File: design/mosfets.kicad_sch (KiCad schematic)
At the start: 26 parts, among them Q1 IRFS7530, Q2 IRFS7530, Q3 IRFS7530, Q4 IRFS7530, Q5 IRFS7530, Q6 IRFS7530, U4 INA826AIDR, U6 OPA333AIDBVR, U7 INA826AIDR

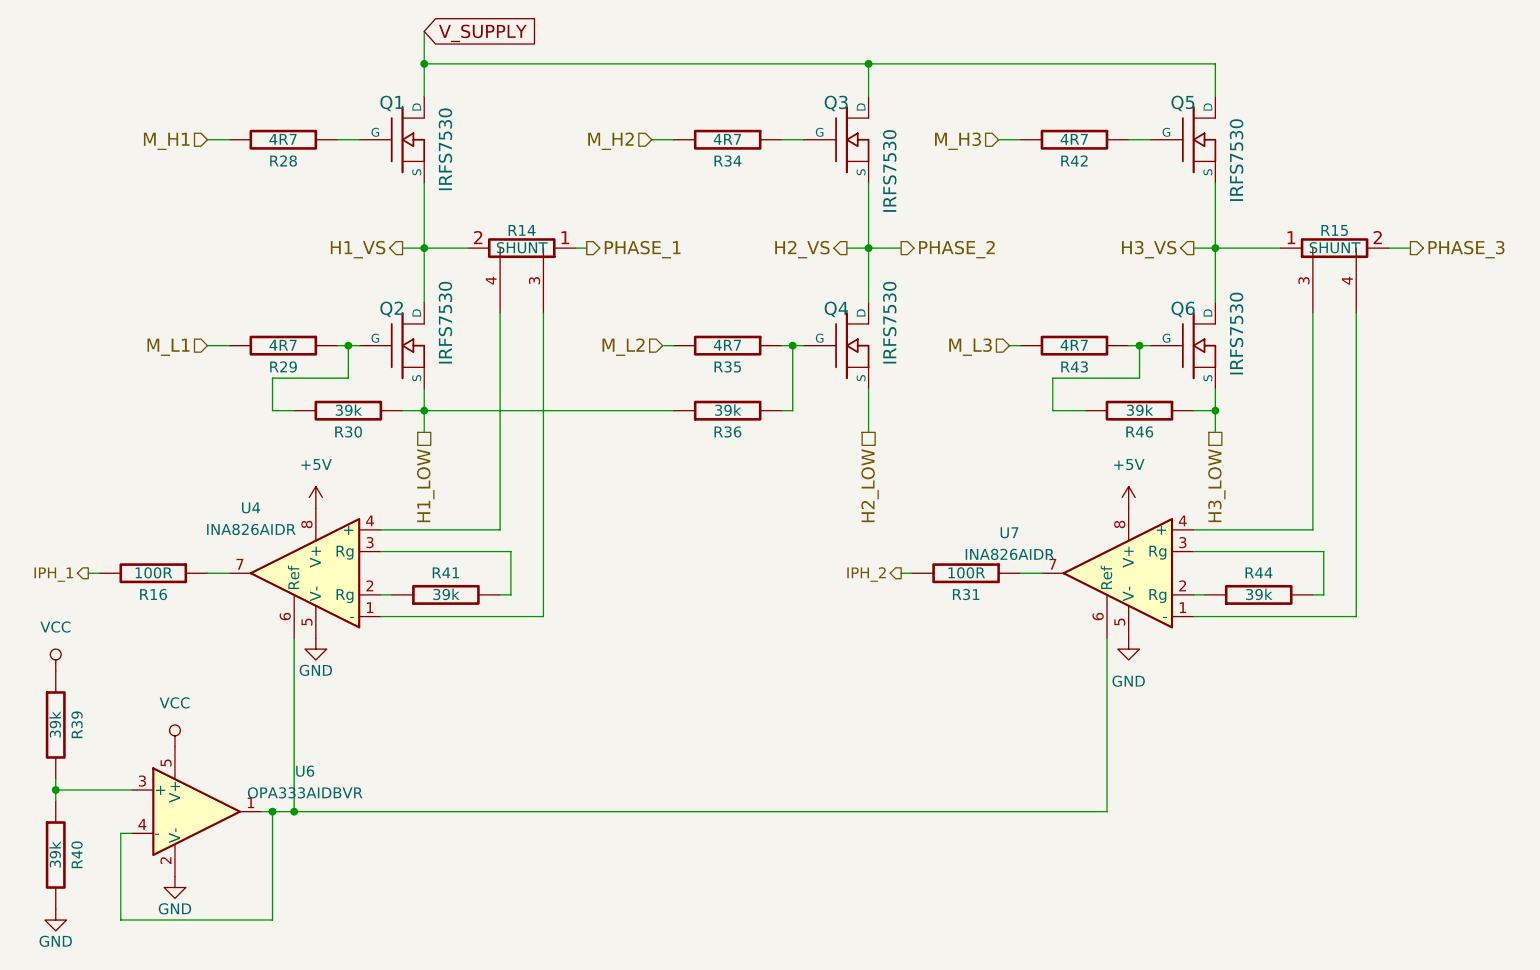
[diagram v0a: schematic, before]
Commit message: STM pins connected
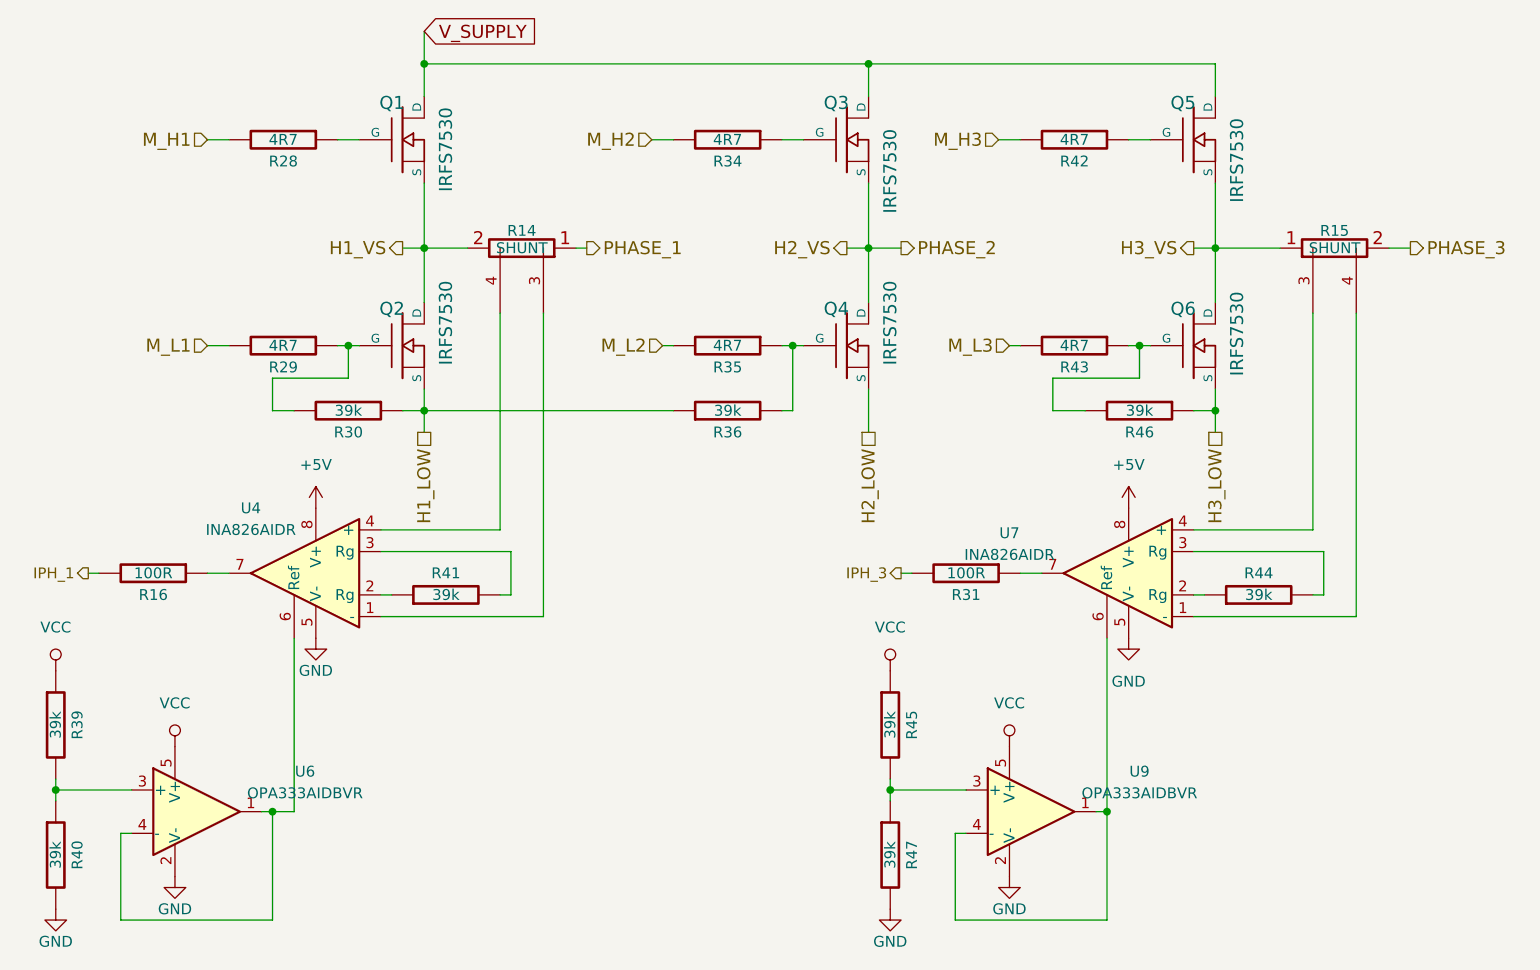
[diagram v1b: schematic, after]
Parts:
- added R45, R47: 39k, CRF1:SMD-0603_r, symbol BLDC_4-rescue:R-RESCUE-BLDC_4
- added U9: OPA333AIDBVR, Package_TO_SOT_SMD:SOT-23-5, symbol Amplifier_Operational:OPA333xxDBV
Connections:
- net GND: now also R47.2, U9.2 (V-)
- net VCC: now also R45.1, U9.5 (V+)
- net at U4.6 (Ref), U6.1, U6.4 (-): no longer U7.6 (Ref)
- net IPH_2 renamed IPH_3
- new net: U7.6 (Ref), U9.1, U9.4 (-)
- new net: R45.2, R47.1, U9.3 (+)

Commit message: Final 20230228
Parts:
- removed R14, R15: SHUNT, CRF1:WSLP2726, symbol BLDC_4-rescue:SHUNT
- added JP8 (x4): SolderJumper_2_Bridged, JRM_Footprint:MicroNetSep, symbol Jumper:SolderJumper_2_Bridged
- added R53 (x2): YLR12-3-8F-W, JRM_Footprint:YLR2512_G4, symbol Device:R_US
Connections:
- net H1_VS: now also JP8.2 (B), R53.1
- net H3_VS: now also JP8.2 (B), R53.1
- net PHASE_1: now also JP8.2 (B), R53.2
- net PHASE_3: now also JP8.2 (B), R53.2
- net at U7.1 (-): now also JP8.1 (A)
- net at U7.4 (+): now also JP8.1 (A)
- net at U4.1 (-): now also JP8.1 (A)
- net at U4.4 (+): now also JP8.1 (A)
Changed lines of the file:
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@@
     (company "Benjamin Vedder")
   )
+  (junction (at 123.19 83.82) (diameter 0) (color 0 0 0 0)
+  )
   (junction (at 115.57 102.87) (diameter 0) (color 0 0 0 0)
   )
@@
   (junction (at 115.57 83.82) (diameter 0) (color 0 0 0 0)
   )
+  (junction (at 130.81 83.82) (diameter 0) (color 0 0 0 0)
+  )
+  (junction (at 218.44 83.82) (diameter 0) (color 0 0 0 0)
+  )
   (junction (at 115.57 62.23) (diameter 0) (color 0 0 0 0)
   )
@@
   (junction (at 167.64 62.23) (diameter 0) (color 0 0 0 0)
   )
+  (junction (at 226.06 83.82) (diameter 0) (color 0 0 0 0)
+  )
   (junction (at 199.39 95.25) (diameter 0) (color 0 0 0 0)
   )
@@
     (stroke (width 0) (type default))
   )
+  (wire (pts (xy 123.19 91.44) (xy 124.46 91.44))
+    (stroke (width 0) (type default))
+  )
   (wire (pts (xy 208.28 102.87) (xy 208.28 105.41))
     (stroke (width 0) (type default))
@@
     (stroke (width 0) (type default))
   )
+  (wire (pts (xy 219.71 91.44) (xy 218.44 91.44))
+    (stroke (width 0) (type default))
+  )
   (wire (pts (xy 170.18 147.32) (xy 170.18 148.59))
     (stroke (width 0) (type default))
@@
     (stroke (width 0) (type default))
   )
+  (wire (pts (xy 224.79 91.44) (xy 226.06 91.44))
+    (stroke (width 0) (type default))
+  )
   (wire (pts (xy 76.2 121.92) (xy 77.47 121.92))
     (stroke (width 0) (type default))
@@
     (stroke (width 0) (type default))
   )
-  (wire (pts (xy 228.6 83.82) (xy 231.14 83.82))
+  (wire (pts (xy 226.06 83.82) (xy 231.14 83.82))
     (stroke (width 0) (type default))
   )
@@
     (stroke (width 0) (type default))
   )
+  (wire (pts (xy 129.54 91.44) (xy 130.81 91.44))
+    (stroke (width 0) (type default))
+  )
   (wire (pts (xy 125.73 124.46) (xy 124.46 124.46))
     (stroke (width 0) (type default))
@@
     (stroke (width 0) (type default))
   )
-  (wire (pts (xy 133.35 83.82) (xy 134.62 83.82))
+  (wire (pts (xy 130.81 83.82) (xy 134.62 83.82))
     (stroke (width 0) (type default))
   )
@@
     (stroke (width 0) (type default))
   )
-  (wire (pts (xy 208.28 83.82) (xy 215.9 83.82))
+  (wire (pts (xy 208.28 83.82) (xy 218.44 83.82))
     (stroke (width 0) (type default))
   )
@@
     (stroke (width 0) (type default))
   )
-  (wire (pts (xy 115.57 83.82) (xy 120.65 83.82))
+  (wire (pts (xy 115.57 83.82) (xy 123.19 83.82))
     (stroke (width 0) (type default))
   )
@@
     )
   )
+  (symbol (lib_id "Jumper:SolderJumper_2_Bridged") (at 123.19 87.63 90) (unit 1)
+    (in_bom yes) (on_board yes) (dnp no)
+    (property "Reference" "JP8" (at 125.73 87.63 0)
+      (effects (font (size 1.27 1.27)))
+    )
+    (property "Value" "SolderJumper_2_Bridged" (at 120.65 87.63 0)
+      (effects (font (size 1.27 1.27)) hide)
+    )
+    (property "Footprint" "JRM_Footprint:MicroNetSep" (at 123.19 87.63 0)
+      (effects (font (size 1.27 1.27)) hide)
+    )
+    (property "Datasheet" "~" (at 123.19 87.63 0)
+      (effects (font (size 1.27 1.27)) hide)
+    )
+    (pin "1")
+    (pin "2")
+    (instances
+      (project "BLDC_4"
+        (path "/f0823096-6b01-491e-b593-a00aa44575f0"
+          (reference "JP8") (unit 1)
+        )
+        (path "/f0823096-6b01-491e-b593-a00aa44575f0/00000000-0000-0000-0000-000053f826dc"
+          (reference "JP12") (unit 1)
+        )
+      )
+    )
+  )
   (symbol (lib_id "power:GND") (at 198.12 129.54 0) (unit 1)
     (in_bom yes) (on_board yes) (dnp no) (fields_autoplaced)
@@
     )
   )
-  (symbol (lib_id "BLDC_4-rescue:SHUNT") (at 127 83.82 270) (mirror x) (unit 1)
-    (in_bom yes) (on_board yes) (dnp no)
-    (property "Reference" "R14" (at 127 81.788 90)
-      (effects (font (size 1.27 1.27)))
-    )
-    (property "Value" "SHUNT" (at 127 83.82 90)
-      (effects (font (size 1.27 1.27)))
-    )
-    (property "Footprint" "CRF1:WSLP2726" (at 127 83.82 0)
-      (effects (font (size 1.524 1.524)) hide)
-    )
-    (property "Datasheet" "" (at 127 83.82 0)
-      (effects (font (size 1.524 1.524)) hide)
-    )
-    (pin "1")
-    (pin "2")
-    (pin "3")
-    (pin "4")
-    (instances
-      (project "BLDC_4"
-        (path "/f0823096-6b01-491e-b593-a00aa44575f0/00000000-0000-0000-0000-000053f826dc"
-          (reference "R14") (unit 1)
-        )
-      )
-    )
-  )
   (symbol (lib_id "Amplifier_Operational:OPA333xxDBV") (at 88.9 149.86 0) (unit 1)
     (in_bom yes) (on_board yes) (dnp no) (fields_autoplaced)
@@
     )
   )
+  (symbol (lib_id "Device:R_US") (at 127 83.82 90) (unit 1)
+    (in_bom yes) (on_board yes) (dnp no) (fields_autoplaced)
+    (property "Reference" "R53" (at 127 78.74 90)
+      (effects (font (size 1.27 1.27)))
+    )
+    (property "Value" "YLR12-3-8F-W" (at 127 81.28 90)
+      (effects (font (size 1.27 1.27)))
+    )
+    (property "Footprint" "JRM_Footprint:YLR2512_G4" (at 127.254 82.804 90)
+      (effects (font (size 1.27 1.27)) hide)
+    )
+    (property "Datasheet" "~" (at 127 83.82 0)
+      (effects (font (size 1.27 1.27)) hide)
+    )
+    (pin "1")
+    (pin "2")
+    (instances
+      (project "BLDC_4"
+        (path "/f0823096-6b01-491e-b593-a00aa44575f0"
+          (reference "R53") (unit 1)
+        )
+        (path "/f0823096-6b01-491e-b593-a00aa44575f0/00000000-0000-0000-0000-000053f826dc"
+          (reference "R14") (unit 1)
+        )
+      )
+    )
+  )
   (symbol (lib_id "BLDC_4-rescue:+5V") (at 198.12 114.3 0) (unit 1)
     (in_bom yes) (on_board yes) (dnp no) (fields_autoplaced)
@@
     )
   )
-  (symbol (lib_id "BLDC_4-rescue:SHUNT") (at 222.25 83.82 90) (unit 1)
-    (in_bom yes) (on_board yes) (dnp no)
-    (property "Reference" "R15" (at 222.25 81.788 90)
-      (effects (font (size 1.27 1.27)))
-    )
-    (property "Value" "SHUNT" (at 222.25 83.82 90)
-      (effects (font (size 1.27 1.27)))
-    )
-    (property "Footprint" "CRF1:WSLP2726" (at 222.25 83.82 0)
-      (effects (font (size 1.524 1.524)) hide)
-    )
-    (property "Datasheet" "" (at 222.25 83.82 0)
-      (effects (font (size 1.524 1.524)) hide)
-    )
-    (pin "1")
-    (pin "2")
-    (pin "3")
-    (pin "4")
-    (instances
-      (project "BLDC_4"
+  (symbol (lib_id "Device:R_US") (at 222.25 83.82 90) (unit 1)
+    (in_bom yes) (on_board yes) (dnp no) (fields_autoplaced)
+    (property "Reference" "R53" (at 222.25 78.74 90)
+      (effects (font (size 1.27 1.27)))
+    )
+    (property "Value" "YLR12-3-8F-W" (at 222.25 81.28 90)
+      (effects (font (size 1.27 1.27)))
+    )
+    (property "Footprint" "JRM_Footprint:YLR2512_G4" (at 222.504 82.804 90)
+      (effects (font (size 1.27 1.27)) hide)
+    )
+    (property "Datasheet" "~" (at 222.25 83.82 0)
+      (effects (font (size 1.27 1.27)) hide)
+    )
+    (pin "1")
+    (pin "2")
+    (instances
+      (project "BLDC_4"
+        (path "/f0823096-6b01-491e-b593-a00aa44575f0"
+          (reference "R53") (unit 1)
+        )
         (path "/f0823096-6b01-491e-b593-a00aa44575f0/00000000-0000-0000-0000-000053f826dc"
           (reference "R15") (unit 1)
@@
     )
   )
+  (symbol (lib_id "Jumper:SolderJumper_2_Bridged") (at 130.81 87.63 90) (unit 1)
+    (in_bom yes) (on_board yes) (dnp no)
+    (property "Reference" "JP8" (at 133.35 87.63 0)
+      (effects (font (size 1.27 1.27)))
+    )
+    (property "Value" "SolderJumper_2_Bridged" (at 128.27 87.63 0)
+      (effects (font (size 1.27 1.27)) hide)
+    )
+    (property "Footprint" "JRM_Footprint:MicroNetSep" (at 130.81 87.63 0)
+      (effects (font (size 1.27 1.27)) hide)
+    )
+    (property "Datasheet" "~" (at 130.81 87.63 0)
+      (effects (font (size 1.27 1.27)) hide)
+    )
+    (pin "1")
+    (pin "2")
+    (instances
+      (project "BLDC_4"
+        (path "/f0823096-6b01-491e-b593-a00aa44575f0"
+          (reference "JP8") (unit 1)
+        )
+        (path "/f0823096-6b01-491e-b593-a00aa44575f0/00000000-0000-0000-0000-000053f826dc"
+          (reference "JP11") (unit 1)
+        )
+      )
+    )
+  )
   (symbol (lib_id "power:GND") (at 102.87 129.54 0) (unit 1)
     (in_bom yes) (on_board yes) (dnp no)
@@
         (path "/f0823096-6b01-491e-b593-a00aa44575f0/00000000-0000-0000-0000-000053f826dc"
           (reference "#PWR078") (unit 1)
+        )
+      )
+    )
+  )
+  (symbol (lib_id "Jumper:SolderJumper_2_Bridged") (at 218.44 87.63 90) (unit 1)
+    (in_bom yes) (on_board yes) (dnp no)
+    (property "Reference" "JP8" (at 220.98 87.63 0)
+      (effects (font (size 1.27 1.27)))
+    )
+    (property "Value" "SolderJumper_2_Bridged" (at 215.9 87.63 0)
+      (effects (font (size 1.27 1.27)) hide)
+    )
+    (property "Footprint" "JRM_Footprint:MicroNetSep" (at 218.44 87.63 0)
+      (effects (font (size 1.27 1.27)) hide)
+    )
+    (property "Datasheet" "~" (at 218.44 87.63 0)
+      (effects (font (size 1.27 1.27)) hide)
+    )
+    (pin "1")
+    (pin "2")
+    (instances
+      (project "BLDC_4"
+        (path "/f0823096-6b01-491e-b593-a00aa44575f0"
+          (reference "JP8") (unit 1)
+        )
+        (path "/f0823096-6b01-491e-b593-a00aa44575f0/00000000-0000-0000-0000-000053f826dc"
+          (reference "JP9") (unit 1)
         )
       )
@@
         )
       )
+    )
+  )
+  (symbol (lib_id "Jumper:SolderJumper_2_Bridged") (at 226.06 87.63 90) (unit 1)
+    (in_bom yes) (on_board yes) (dnp no)
+    (property "Reference" "JP8" (at 228.6 87.63 0)
+      (effects (font (size 1.27 1.27)))
+    )
+    (property "Value" "SolderJumper_2_Bridged" (at 223.52 87.63 0)
+      (effects (font (size 1.27 1.27)) hide)
+    )
+    (property "Footprint" "JRM_Footprint:MicroNetSep" (at 226.06 87.63 0)
+      (effects (font (size 1.27 1.27)) hide)
+    )
+    (property "Datasheet" "~" (at 226.06 87.63 0)
+      (effects (font (size 1.27 1.27)) hide)
+    )
+    (pin "1")
+    (pin "2")
+    (instances
+      (project "BLDC_4"
+        (path "/f0823096-6b01-491e-b593-a00aa44575f0"
+          (reference "JP8") (unit 1)
+        )
+        (path "/f0823096-6b01-491e-b593-a00aa44575f0/00000000-0000-0000-0000-000053f826dc"
+          (reference "JP10") (unit 1)
+        )
+      )
